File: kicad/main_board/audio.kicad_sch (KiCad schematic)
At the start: 60 parts, among them J7 MIC, J8 LINE_ALT, J9 LINE, Q5 DMG1013UW, U10 MCP6002, U11 MCP6002, U9 MCP4451-503

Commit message: add charger
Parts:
- C74: renamed from C39; LCSC (none) -> C1589; MPN_ALT C1589 -> (none)
- C75: renamed from C40; LCSC (none) -> C1589; MPN_ALT C1589 -> (none)
- C76: renamed from C41; LCSC (none) -> C1589; MPN_ALT C1589 -> (none)
- renumbered C32 to C67, C33 to C68, C34 to C69, C35 to C70, C36 to C71, C37 to C72, C38 to C73, C42 to C77, C43 to C78, C44 to C79, C45 to C80, C46 to C81, C47 to C82, C48 to C83, C49 to C84, C50 to C85, D9 to D10, D10 to D11, D8 to D9, J8 to J10, J9 to J11, J7 to J9, Q5 to Q10, R39 to R58, R40 to R59, R41 to R60, R42 to R61, R43 to R62, R44 to R63, R45 to R64, R46 to R65, R47 to R66, R48 to R67, R49 to R68, R50 to R69, R51 to R70, R52 to R71, R53 to R72, R54 to R73, R55 to R74, R56 to R75, R57 to R76, R58 to R77, R59 to R78, R60 to R79, R61 to R80, R62 to R81, R63 to R82, TP25 to TP32, TP26 to TP33, TP27 to TP34, TP28 to TP35, TP29 to TP36, U9 to U10, U10 to U11, U11 to U12

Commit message: add I2S link
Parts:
- renumbered TP32 to TP31, TP33 to TP32, TP34 to TP33, TP35 to TP34, TP36 to TP35
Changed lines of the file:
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@@
 	(title_block
 		(title "SW32 - Main Board")
-		(date "2024-05-22")
+		(date "2024-05-23")
 		(rev "1")
 		(company "saawsm")
@@
 		(dnp no)
 		(fields_autoplaced yes)
-		(property "Reference" "TP33"
+		(property "Reference" "TP32"
 			(at 82.55 171.45 90)
 			(effects
@@
 			(project "main_board"
 				(path "/8e1f1504-76c2-49e6-9261-3c1190503f8c/62c05929-ef0a-4f70-9eff-4dad203c33f9"
-					(reference "TP33")
+					(reference "TP32")
 					(unit 1)
 				)
@@
 		(dnp no)
 		(fields_autoplaced yes)
-		(property "Reference" "TP36"
+		(property "Reference" "TP35"
 			(at 275.59 113.03 0)
 			(effects
@@
 			(project "main_board"
 				(path "/8e1f1504-76c2-49e6-9261-3c1190503f8c/62c05929-ef0a-4f70-9eff-4dad203c33f9"
-					(reference "TP36")
+					(reference "TP35")
 					(unit 1)
 				)
@@
 		(dnp no)
 		(fields_autoplaced yes)
-		(property "Reference" "TP32"
+		(property "Reference" "TP31"
 			(at 59.69 180.34 0)
 			(effects
@@
 			(project "main_board"
 				(path "/8e1f1504-76c2-49e6-9261-3c1190503f8c/62c05929-ef0a-4f70-9eff-4dad203c33f9"
-					(reference "TP32")
+					(reference "TP31")
 					(unit 1)
 				)
@@
 		(dnp no)
 		(fields_autoplaced yes)
-		(property "Reference" "TP35"
+		(property "Reference" "TP34"
 			(at 180.34 102.87 90)
 			(effects
@@
 			(project "main_board"
 				(path "/8e1f1504-76c2-49e6-9261-3c1190503f8c/62c05929-ef0a-4f70-9eff-4dad203c33f9"
-					(reference "TP35")
+					(reference "TP34")
 					(unit 1)
 				)
@@
 		(dnp no)
 		(fields_autoplaced yes)
-		(property "Reference" "TP34"
+		(property "Reference" "TP33"
 			(at 177.8 29.21 90)
 			(effects
@@
 			(project "main_board"
 				(path "/8e1f1504-76c2-49e6-9261-3c1190503f8c/62c05929-ef0a-4f70-9eff-4dad203c33f9"
-					(reference "TP34")
+					(reference "TP33")
 					(unit 1)
 				)

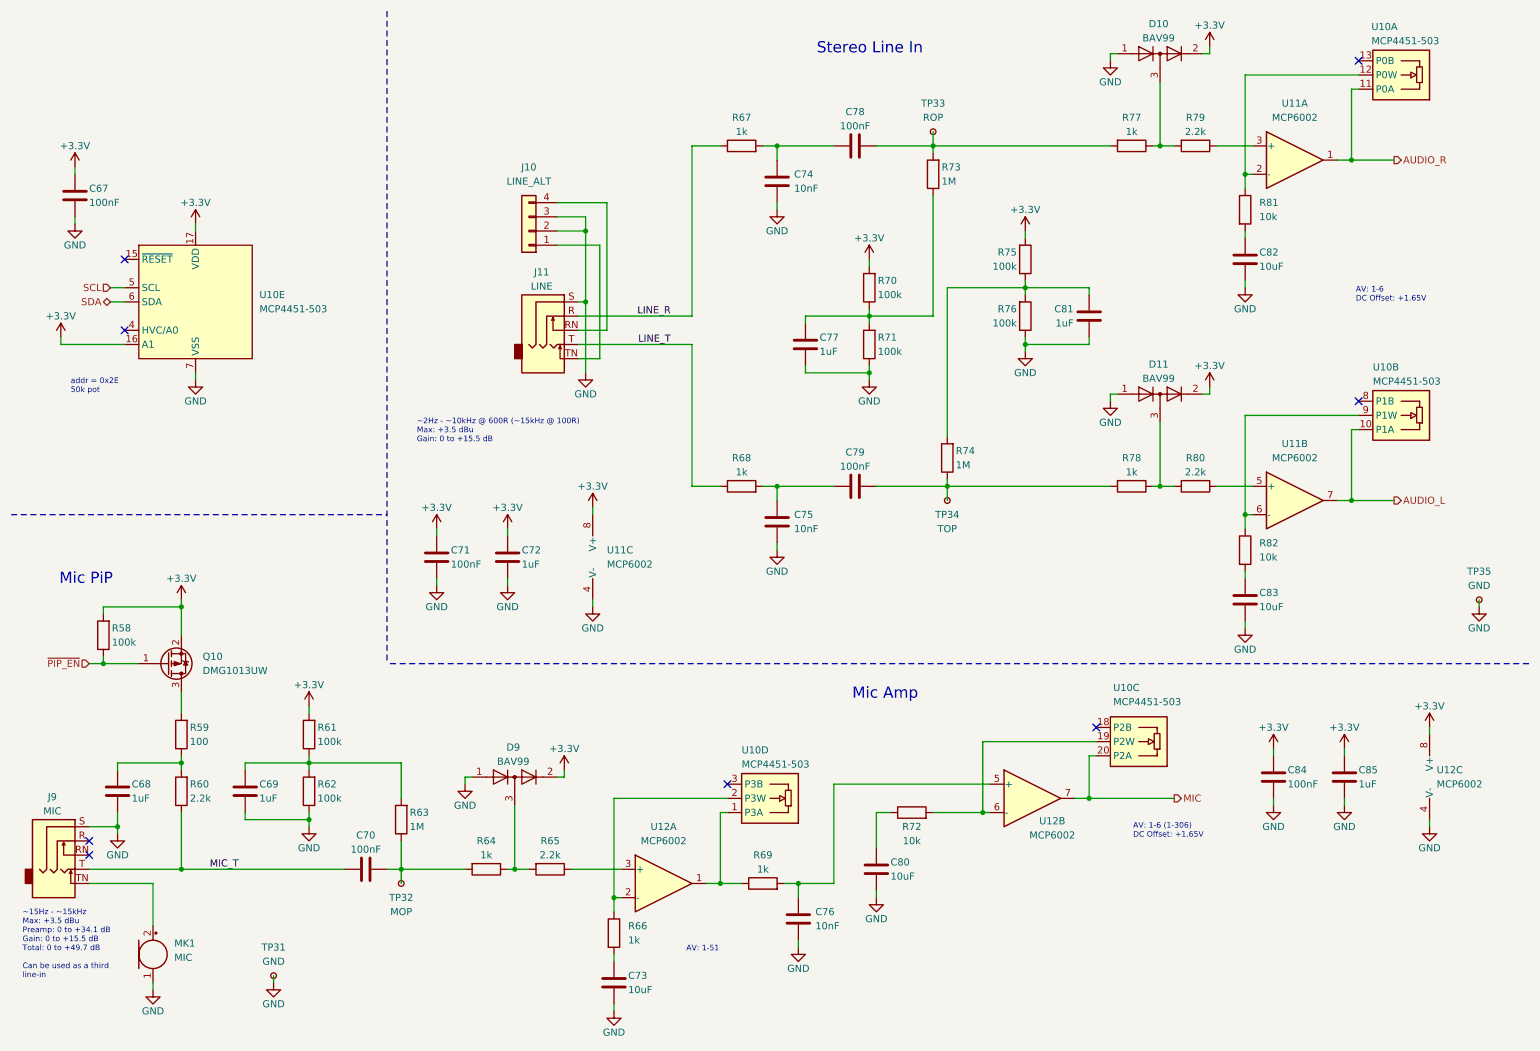
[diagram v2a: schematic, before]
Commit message: remove BAT_INT
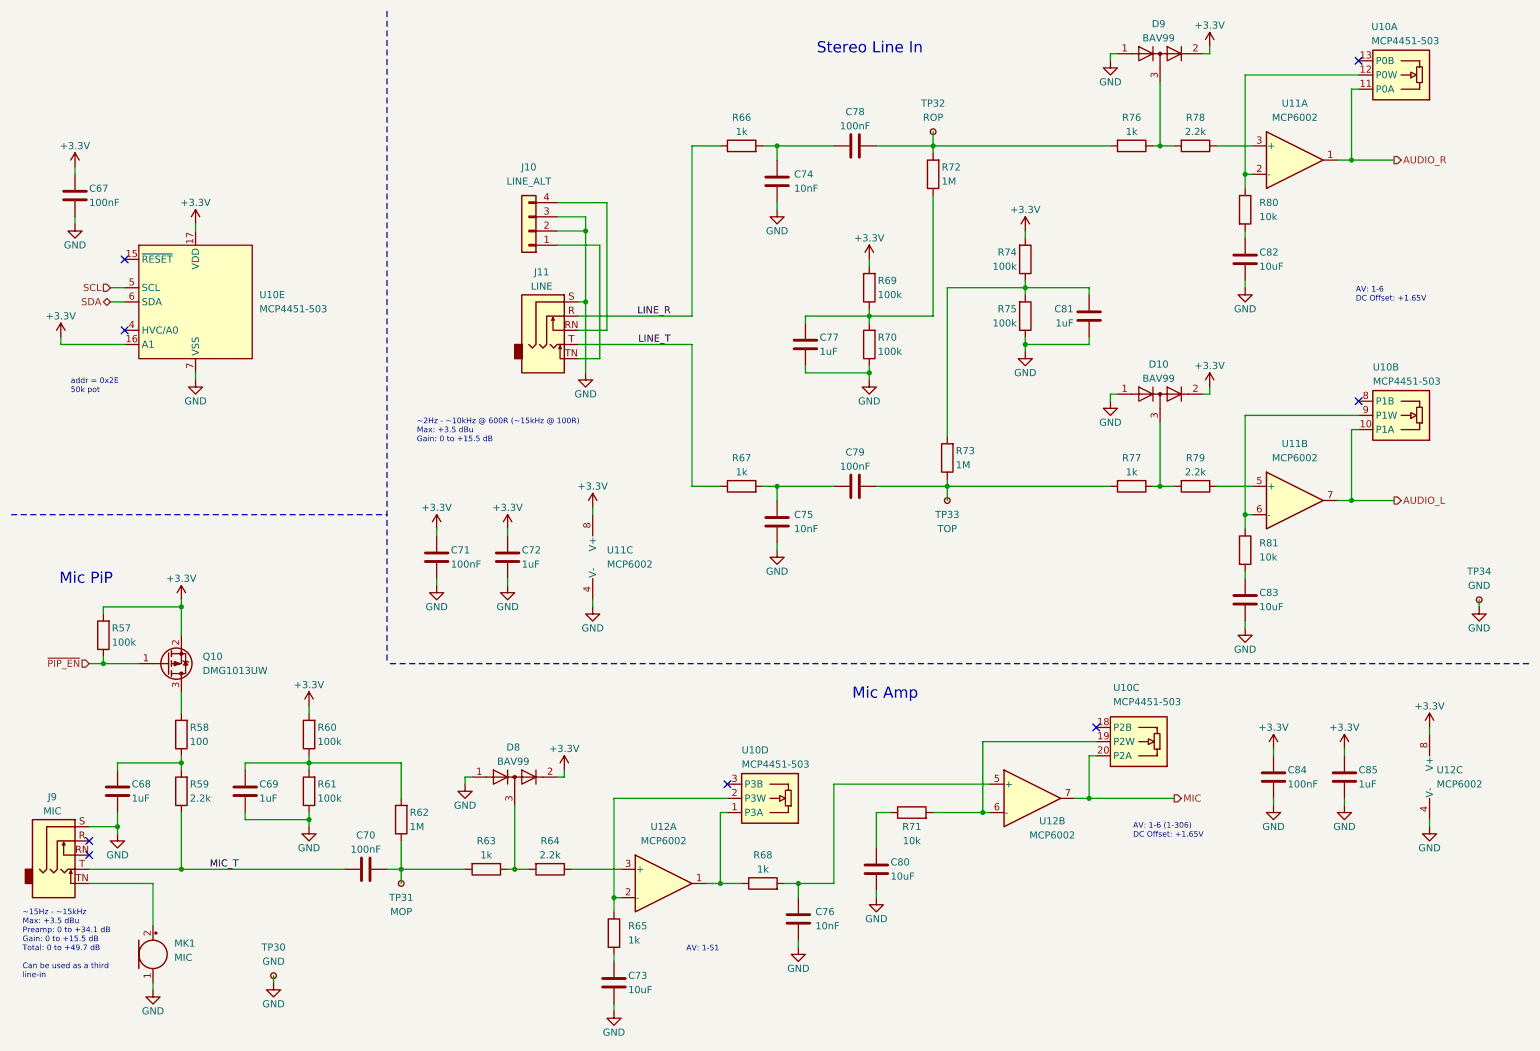
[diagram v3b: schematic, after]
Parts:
- renumbered D11 to D10, D9 to D8, D10 to D9, R58 to R57, R59 to R58, R60 to R59, R61 to R60, R62 to R61, R63 to R62, R64 to R63, R65 to R64, R66 to R65, R67 to R66, R68 to R67, R69 to R68, R70 to R69, R71 to R70, R72 to R71, R73 to R72, R74 to R73, R75 to R74, R76 to R75, R77 to R76, R78 to R77, R79 to R78, R80 to R79, R81 to R80, R82 to R81, TP31 to TP30, TP32 to TP31, TP33 to TP32, TP34 to TP33, TP35 to TP34

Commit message: update BOM prioritizing basic parts
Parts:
- C67, C70, C71, C78, C79, C84: JLC (none) -> C14663; LCSC C1591 -> (none); MOUSER 187-CL10B104KB8NNNC -> (none); MPN CL10B104KB8NNNC -> (none)
- C68, C69, C72, C77, C81, C85: JLC (none) -> C15849; LCSC C5199872 -> (none); MOUSER 187-CL10B105KB8NQNC -> (none); MPN CL10B105KB8NQNC -> (none)
- C73, C80, C82, C83: JLC (none) -> C96446; LCSC C96446 -> (none); MOUSER 187-CL10A106MA8NRNC -> (none); MPN CL10A106MA8NRNC -> (none)
- C74, C75, C76: JLC (none) -> C57112; LCSC C1589 -> (none); MOUSER 187-CL10B103KB8NNNC -> (none); MPN CL10B103KB8NNNC -> (none)
- D10, D8, D9: footprint Package_TO_SOT_SMD:SOT-323_SC-70 -> Package_TO_SOT_SMD:SOT-23; JLC (none) -> C2500; LCSC C93035 -> (none); MOUSER 621-BAV99W-F -> (none); MPN BAV99W-7-F -> (none)
- J10: LCSC (none) -> C2691448
- J11, J9: footprint SaawLib:STX-3100-5N -> SaawLib:PJ-3062-CO; LCSC (none) -> C319113; MOUSER 806-STX-3100-5N -> (none); MPN STX-3100-5N -> (none)
- MK1: JLC (none) -> C3273723; LCSC C3273723 -> (none); MOUSER 490CMC-4013-2-SMT-TR -> (none); MPN CMC-4013-2-SMT-TR -> (none)
- Q10: value DMG1013UW -> AO3401A; footprint Package_TO_SOT_SMD:SOT-323_SC-70 -> Package_TO_SOT_SMD:SOT-23; JLC (none) -> C15127; LCSC C211434 -> (none); MOUSER 621-DMG1013UW-7 -> (none); MPN DMG1013UW-7 -> (none)
- R57, R60, R61, R69, R70, R74, R75: JLC (none) -> C25803; LCSC C25803 -> (none); MOUSER 603-RC0603FR-07100KL -> (none); MPN RC0603FR-07100KL -> (none)
- R58: JLC (none) -> C22775; LCSC C22775 -> (none); MOUSER 603-RC0603FR-13100RL -> (none); MPN RC0603FR-07100RL -> (none)
- R59, R64, R78, R79: JLC (none) -> C4190; LCSC C4190 -> (none); MOUSER 603-RC0603FR-072K2L -> (none); MPN RC0603FR-072K2L -> (none)
- R62, R72, R73: JLC (none) -> C22935; LCSC C22935 -> (none); MOUSER 603-RC0603FR-071ML -> (none); MPN RC0603FR-071ML -> (none)
- R63, R65, R66, R67, R68, R76, R77: JLC (none) -> C21190; LCSC C21190 -> (none); MOUSER 603-RC0603FR-071KL -> (none); MPN RC0603FR-071KL -> (none)
- R71, R80, R81: JLC (none) -> C25804; LCSC C25804 -> (none); MOUSER 603-RC0603FR-0710KL -> (none); MPN RC0603FR-0710KL -> (none)
- U10: JLC (none) -> C638706; LCSC C638706 -> (none); MOUSER 579-MCP4451-503E/ST -> (none); MPN MCP4451-503E/ST -> (none)
- U11, U12: JLC (none) -> C2652308; LCSC C2652308 -> (none); MOUSER 579-MCP6002T-I/MS -> (none); MPN MCP6002T-I/MS -> (none)

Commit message: add generation script
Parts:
- C67, C70, C71, C78, C79, C84: JLC C14663 -> (none); LCSC (none) -> C14663; Service (none) -> PCBA
- C68, C69, C72, C77, C81, C85: JLC C15849 -> (none); LCSC (none) -> C15849; Service (none) -> PCBA
- C73, C80, C82, C83: JLC C96446 -> (none); LCSC (none) -> C96446; Service (none) -> PCBA
- C74, C75, C76: JLC C57112 -> (none); LCSC (none) -> C57112; Service (none) -> PCBA
- D10, D8, D9: JLC C2500 -> (none); LCSC (none) -> C2500; Service (none) -> PCBA
- J10, J11, J9: Service (none) -> HandAssembly
- MK1: JLC C3273723 -> (none); LCSC (none) -> C3273723; Service (none) -> PCBA
- Q10: JLC C15127 -> (none); LCSC (none) -> C15127; Service (none) -> PCBA
- R57, R60, R61, R69, R70, R74, R75: JLC C25803 -> (none); LCSC (none) -> C25803; Service (none) -> PCBA
- R58: JLC C22775 -> (none); LCSC (none) -> C22775; Service (none) -> PCBA
- R59, R64, R78, R79: JLC C4190 -> (none); LCSC (none) -> C4190; Service (none) -> PCBA
- R62, R72, R73: JLC C22935 -> (none); LCSC (none) -> C22935; Service (none) -> PCBA
- R63, R65, R66, R67, R68, R76, R77: JLC C21190 -> (none); LCSC (none) -> C21190; Service (none) -> PCBA
- R71, R80, R81: JLC C25804 -> (none); LCSC (none) -> C25804; Service (none) -> PCBA
- TP30, TP31, TP32, TP33, TP34: Service (none) -> PCBA;HandAssembly
- U10: JLC C638706 -> (none); LCSC (none) -> C638706; Service (none) -> PCBA
- U11, U12: JLC C2652308 -> (none); LCSC (none) -> C2652308; Service (none) -> PCBA

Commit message: update smd mic bom
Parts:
- MK1: footprint Sensor_Audio:CUI_CMC-4013-SMT -> (none); LCSC C3273723 -> C5160218
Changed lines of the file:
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@@
 			)
 		)
-		(property "Footprint" "Sensor_Audio:CUI_CMC-4013-SMT"
+		(property "Footprint" ""
 			(at 38.1 179.07 90)
 			(effects
@@
 			)
 		)
-		(property "Datasheet" "https://www.cuidevices.com/product/resource/cmc-4013-2-smt-tr.pdf"
+		(property "Datasheet" "https://www.lcsc.com/datasheet/lcsc_datasheet_2209081730_Goertek-B4013AM423-092_C5160218.pdf"
 			(at 38.1 179.07 90)
 			(effects
@@
 			)
 		)
-		(property "LCSC" "C3273723"
+		(property "LCSC" "C5160218"
 			(at 38.1 181.61 0)
 			(effects

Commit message: add mic footprint
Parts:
- MK1: footprint (none) -> Sensor_Audio:CUI_CMC-4013-SMT
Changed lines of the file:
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@@
 			)
 		)
-		(property "Footprint" ""
+		(property "Footprint" "Sensor_Audio:CUI_CMC-4013-SMT"
 			(at 38.1 179.07 90)
 			(effects
